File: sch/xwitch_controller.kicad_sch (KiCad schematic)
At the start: 30 parts

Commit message: usb2515b ic power and comms circuit
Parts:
- C? (x2): footprint Capacitor_SMD:C_0603_1608Metric_Pad1.08x0.95mm_HandSolder -> Capacitor_SMD:C_0402_1005Metric_Pad0.74x0.62mm_HandSolder; LCSC C1658 -> C1570
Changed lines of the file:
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@@
       (effects (font (size 1.27 1.27)) (justify left))
     )
-    (property "Footprint" "Capacitor_SMD:C_0603_1608Metric_Pad1.08x0.95mm_HandSolder" (id 2) (at 240.9952 140.97 0)
+    (property "Footprint" "Capacitor_SMD:C_0402_1005Metric_Pad0.74x0.62mm_HandSolder" (id 2) (at 240.9952 140.97 0)
       (effects (font (size 1.27 1.27)) hide)
     )
@@
       (effects (font (size 1.27 1.27)) hide)
     )
-    (property "LCSC" "C1658" (id 4) (at 240.03 137.16 0)
+    (property "LCSC" "C1570" (id 4) (at 240.03 137.16 0)
       (effects (font (size 1.27 1.27)) hide)
     )
@@
       (effects (font (size 1.27 1.27)) (justify left))
     )
-    (property "Footprint" "Capacitor_SMD:C_0603_1608Metric_Pad1.08x0.95mm_HandSolder" (id 2) (at 258.7752 140.97 0)
+    (property "Footprint" "Capacitor_SMD:C_0402_1005Metric_Pad0.74x0.62mm_HandSolder" (id 2) (at 258.7752 140.97 0)
       (effects (font (size 1.27 1.27)) hide)
     )
@@
       (effects (font (size 1.27 1.27)) hide)
     )
-    (property "LCSC" "C1658" (id 4) (at 257.81 137.16 0)
+    (property "LCSC" "C1570" (id 4) (at 257.81 137.16 0)
       (effects (font (size 1.27 1.27)) hide)
     )

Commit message: annotated components
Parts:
- removed J?: BOOTSEL, Connector_PinHeader_2.54mm:PinHeader_1x02_P2.54mm_Vertical, symbol Connector:Conn_01x02_Male
- added SW2: C2689642, usb_xwitch:SW_SPST_CK_PTS636_SP43_SMTR, symbol Switch:SW_SPST
- C15: renamed from C?; Field4 C1525 -> (none); LCSC (none) -> C1525
- gave numbers to parts that had none: 28
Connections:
- net GND: now also SW2.1 (A)
- net at R3.2: now also SW2.2 (B)

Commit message: drc checks and renaming
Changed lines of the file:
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@@
 (kicad_sch (version 20211123) (generator eeschema)
   (paper "A4")
+  (junction (at 170.18 25.4) (diameter 0) (color 0 0 0 0)
+  )
   (junction (at 157.48 41.91) (diameter 0) (color 0 0 0 0)
   )
@@
   )
   (junction (at 194.31 33.02) (diameter 0) (color 0 0 0 0)
-  )
-  (junction (at 170.18 25.4) (diameter 0) (color 0 0 0 0)
   )
   (junction (at 234.95 33.02) (diameter 0) (color 0 0 0 0)
@@
     (pin "1")
     (pin "2")
+  )
+  (symbol (lib_id "power:+3V3") (at 77.47 24.13 0) (unit 1)
+    (in_bom yes) (on_board yes)
+    (property "Reference" "#PWR0127" (id 0) (at 77.47 27.94 0)
+      (effects (font (size 1.27 1.27)) hide)
+    )
+    (property "Value" "+3V3" (id 1) (at 74.93 20.32 0)
+      (effects (font (size 1.27 1.27)) (justify left))
+    )
+    (property "Footprint" "" (id 2) (at 77.47 24.13 0)
+      (effects (font (size 1.27 1.27)) hide)
+    )
+    (property "Datasheet" "" (id 3) (at 77.47 24.13 0)
+      (effects (font (size 1.27 1.27)) hide)
+    )
+    (pin "1")
   )
   (symbol (lib_id "power:GND") (at 240.03 142.24 0) (unit 1)
@@
     (pin "1")
   )
-  (symbol (lib_id "power:+3.3V") (at 170.18 25.4 0) (unit 1)
-    (in_bom yes) (on_board yes) (fields_autoplaced)
-    (property "Reference" "#PWR015" (id 0) (at 170.18 29.21 0)
-      (effects (font (size 1.27 1.27)) hide)
-    )
-    (property "Value" "+3.3V" (id 1) (at 170.18 20.32 0))
-    (property "Footprint" "" (id 2) (at 170.18 25.4 0)
-      (effects (font (size 1.27 1.27)) hide)
-    )
-    (property "Datasheet" "" (id 3) (at 170.18 25.4 0)
-      (effects (font (size 1.27 1.27)) hide)
-    )
-    (pin "1")
-  )
   (symbol (lib_id "power:GND") (at 153.67 153.67 0) (unit 1)
     (in_bom yes) (on_board yes) (fields_autoplaced)
@@
     (pin "2")
   )
-  (symbol (lib_id "power:+3.3V") (at 77.47 24.13 0) (unit 1)
-    (in_bom yes) (on_board yes)
-    (property "Reference" "#PWR013" (id 0) (at 77.47 27.94 0)
-      (effects (font (size 1.27 1.27)) hide)
-    )
-    (property "Value" "+3.3V" (id 1) (at 77.47 20.32 0))
-    (property "Footprint" "" (id 2) (at 77.47 24.13 0)
-      (effects (font (size 1.27 1.27)) hide)
-    )
-    (property "Datasheet" "" (id 3) (at 77.47 24.13 0)
-      (effects (font (size 1.27 1.27)) hide)
-    )
-    (pin "1")
-  )
   (symbol (lib_id "power:GND") (at 245.11 34.29 0) (unit 1)
     (in_bom yes) (on_board yes)
@@
     (pin "1")
   )
-  (symbol (lib_id "power:+3.3V") (at 29.21 60.96 0) (unit 1)
-    (in_bom yes) (on_board yes) (fields_autoplaced)
-    (property "Reference" "#PWR024" (id 0) (at 29.21 64.77 0)
-      (effects (font (size 1.27 1.27)) hide)
-    )
-    (property "Value" "+3.3V" (id 1) (at 29.21 55.88 0))
-    (property "Footprint" "" (id 2) (at 29.21 60.96 0)
-      (effects (font (size 1.27 1.27)) hide)
-    )
-    (property "Datasheet" "" (id 3) (at 29.21 60.96 0)
-      (effects (font (size 1.27 1.27)) hide)
-    )
-    (pin "1")
-  )
   (symbol (lib_id "power:+5V") (at 53.34 24.13 0) (mirror y) (unit 1)
     (in_bom yes) (on_board yes)
@@
     (pin "2")
   )
+  (symbol (lib_id "power:+3V3") (at 29.21 60.96 0) (unit 1)
+    (in_bom yes) (on_board yes)
+    (property "Reference" "#PWR0126" (id 0) (at 29.21 64.77 0)
+      (effects (font (size 1.27 1.27)) hide)
+    )
+    (property "Value" "+3V3" (id 1) (at 26.67 57.15 0)
+      (effects (font (size 1.27 1.27)) (justify left))
+    )
+    (property "Footprint" "" (id 2) (at 29.21 60.96 0)
+      (effects (font (size 1.27 1.27)) hide)
+    )
+    (property "Datasheet" "" (id 3) (at 29.21 60.96 0)
+      (effects (font (size 1.27 1.27)) hide)
+    )
+    (pin "1")
+  )
   (symbol (lib_id "Device:C") (at 176.53 39.37 0) (unit 1)
     (in_bom yes) (on_board yes) (fields_autoplaced)
@@
     (pin "2")
   )
+  (symbol (lib_id "power:+3V3") (at 170.18 25.4 0) (unit 1)
+    (in_bom yes) (on_board yes)
+    (property "Reference" "#PWR0128" (id 0) (at 170.18 29.21 0)
+      (effects (font (size 1.27 1.27)) hide)
+    )
+    (property "Value" "+3V3" (id 1) (at 167.64 21.59 0)
+      (effects (font (size 1.27 1.27)) (justify left))
+    )
+    (property "Footprint" "" (id 2) (at 170.18 25.4 0)
+      (effects (font (size 1.27 1.27)) hide)
+    )
+    (property "Datasheet" "" (id 3) (at 170.18 25.4 0)
+      (effects (font (size 1.27 1.27)) hide)
+    )
+    (pin "1")
+  )
   (symbol (lib_id "Regulator_Linear:NCP1117-3.3_SOT223") (at 64.77 25.4 0) (unit 1)

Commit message: updated power on leds, hub 4 LEDs and misc
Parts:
- removed C10, C11: 10u, Capacitor_SMD:C_0603_1608Metric_Pad1.08x0.95mm_HandSolder, symbol Device:C
- removed U1: NCP1117LPST33T3G, Package_TO_SOT_SMD:SOT-223-3_TabPin2, symbol Regulator_Linear:NCP1117-3.3_SOT223
- added TP7: TestPoint, TestPoint:TestPoint_Pad_D1.0mm, symbol Connector:TestPoint
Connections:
- net +1V1: now also TP7.1
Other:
- moved on the sheet: D1, J1

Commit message: component layout all in board
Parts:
- Y1: footprint Crystal:Crystal_SMD_3225-4Pin_3.2x2.5mm_HandSoldering -> Crystal:Crystal_SMD_3225-4Pin_3.2x2.5mm
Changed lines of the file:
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@@
     (property "Reference" "Y1" (id 0) (at 251.46 123.19 0))
     (property "Value" "12MHz" (id 1) (at 252.73 125.73 0))
-    (property "Footprint" "Crystal:Crystal_SMD_3225-4Pin_3.2x2.5mm_HandSoldering" (id 2) (at 248.92 130.81 0)
+    (property "Footprint" "Crystal:Crystal_SMD_3225-4Pin_3.2x2.5mm" (id 2) (at 248.92 130.81 0)
       (effects (font (size 1.27 1.27)) hide)
     )

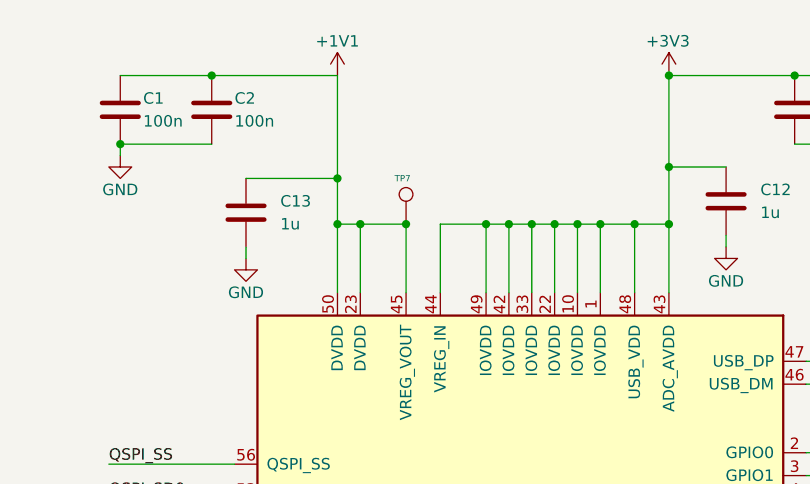
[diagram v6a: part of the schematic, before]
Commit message: rp2040 routing added
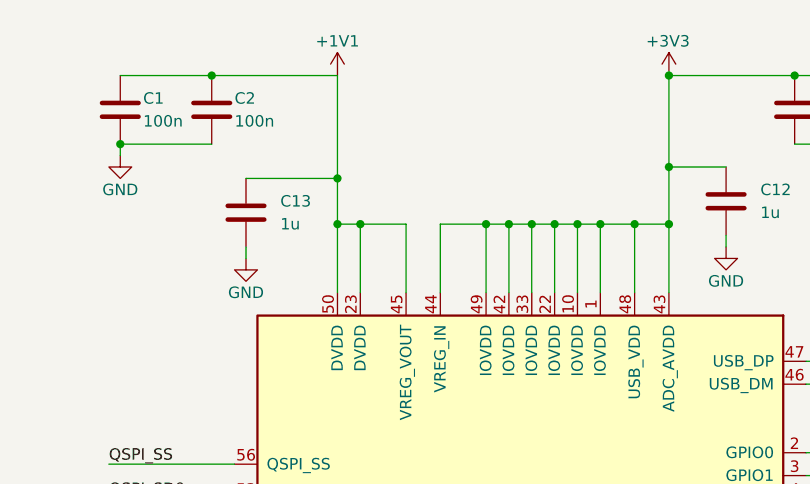
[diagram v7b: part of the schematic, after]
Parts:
- removed TP7: TestPoint, TestPoint:TestPoint_Pad_D1.0mm, symbol Connector:TestPoint
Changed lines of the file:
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@@
   (junction (at 194.31 25.4) (diameter 0) (color 0 0 0 0)
-  )
-  (junction (at 140.97 41.91) (diameter 0) (color 0 0 0 0)
   )
   (junction (at 209.55 130.81) (diameter 0) (color 0 0 0 0)
@@
       (effects (font (size 1.27 1.27)) hide)
     )
-    (pin "1")
-  )
-  (symbol (lib_id "Connector:TestPoint") (at 140.97 41.91 0) (unit 1)
-    (in_bom yes) (on_board yes)
-    (property "Reference" "TP7" (id 0) (at 139.7 36.83 0)
-      (effects (font (size 0.7 0.7)) (justify left))
-    )
-    (property "Value" "TestPoint" (id 1) (at 143.51 39.8779 0)
-      (effects (font (size 1.27 1.27)) (justify left) hide)
-    )
-    (property "Footprint" "TestPoint:TestPoint_Pad_D1.0mm" (id 2) (at 146.05 41.91 0)
-      (effects (font (size 1.27 1.27)) hide)
-    )
-    (property "Datasheet" "~" (id 3) (at 146.05 41.91 0)
-      (effects (font (size 1.27 1.27)) hide)
-    )

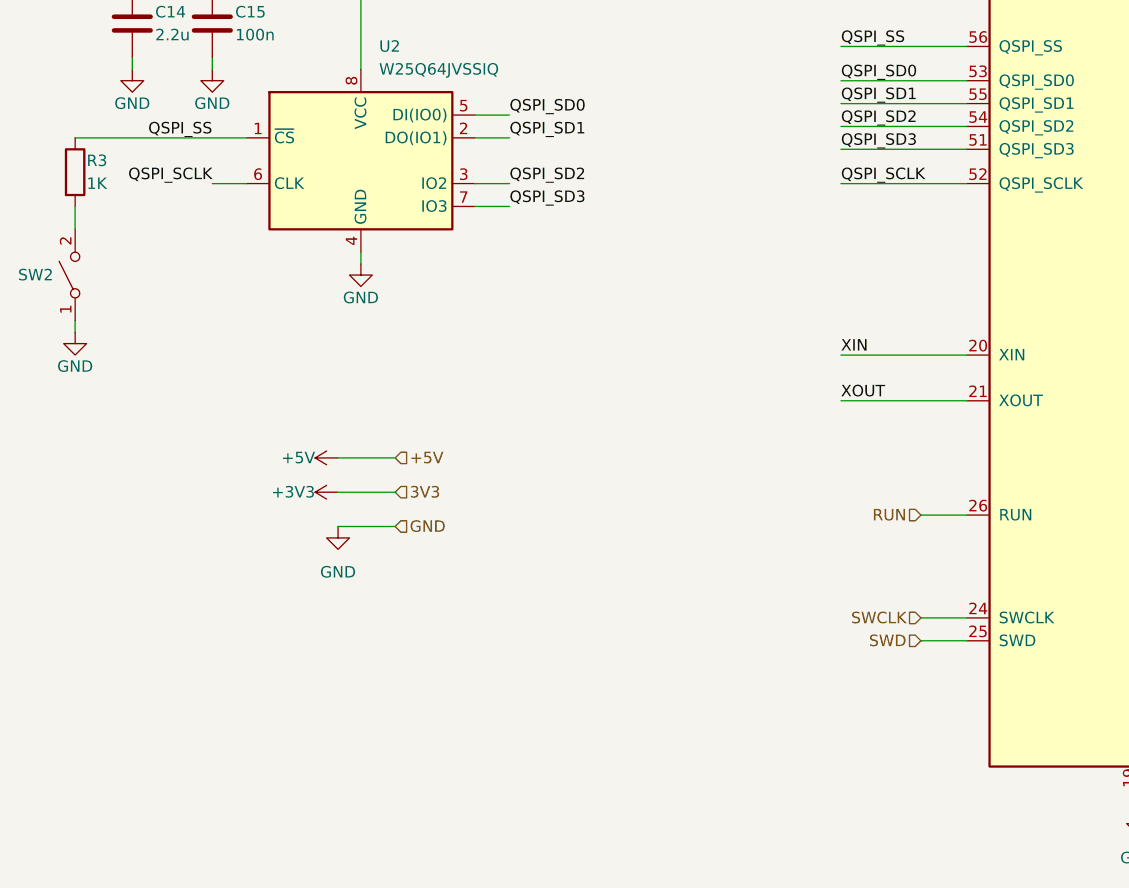
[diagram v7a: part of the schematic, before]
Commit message: added more DNF components for easy debugging
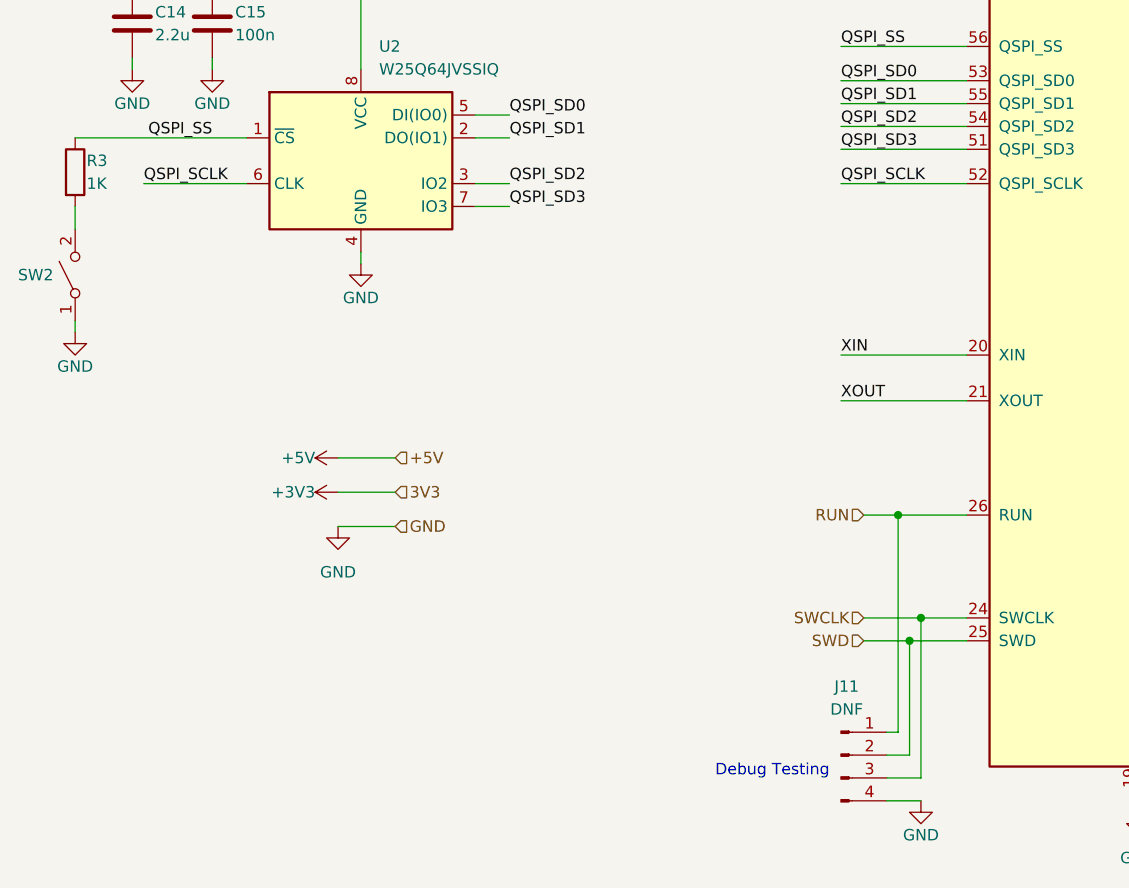
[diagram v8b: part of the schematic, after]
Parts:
- added J11: DNF, Connector_PinHeader_1.00mm:PinHeader_1x04_P1.00mm_Vertical_SMD_Pin1Left, symbol Connector:Conn_01x04_Male
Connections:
- net GND: now also J11.4 (Pin_4)
- net RUN: now also J11.1 (Pin_1)
- net SWCLK: now also J11.3 (Pin_3)
- net SWD: now also J11.2 (Pin_2)
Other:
- note added: "Debug Testing"
